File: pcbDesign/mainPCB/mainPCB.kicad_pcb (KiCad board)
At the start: 4 copper layers, 188.1 x 90 mm, 40 parts, among them CN1 CONN 45P FOR GG 01, CN3 WIRE HARN SP FOR GG, CN4 CN4, SW1 UP, SW2 DOWN, SW3 LEFT, SW4 RIGHT, SW5 TL, SW6 TR, SW7 PS, T1 Transformer T1

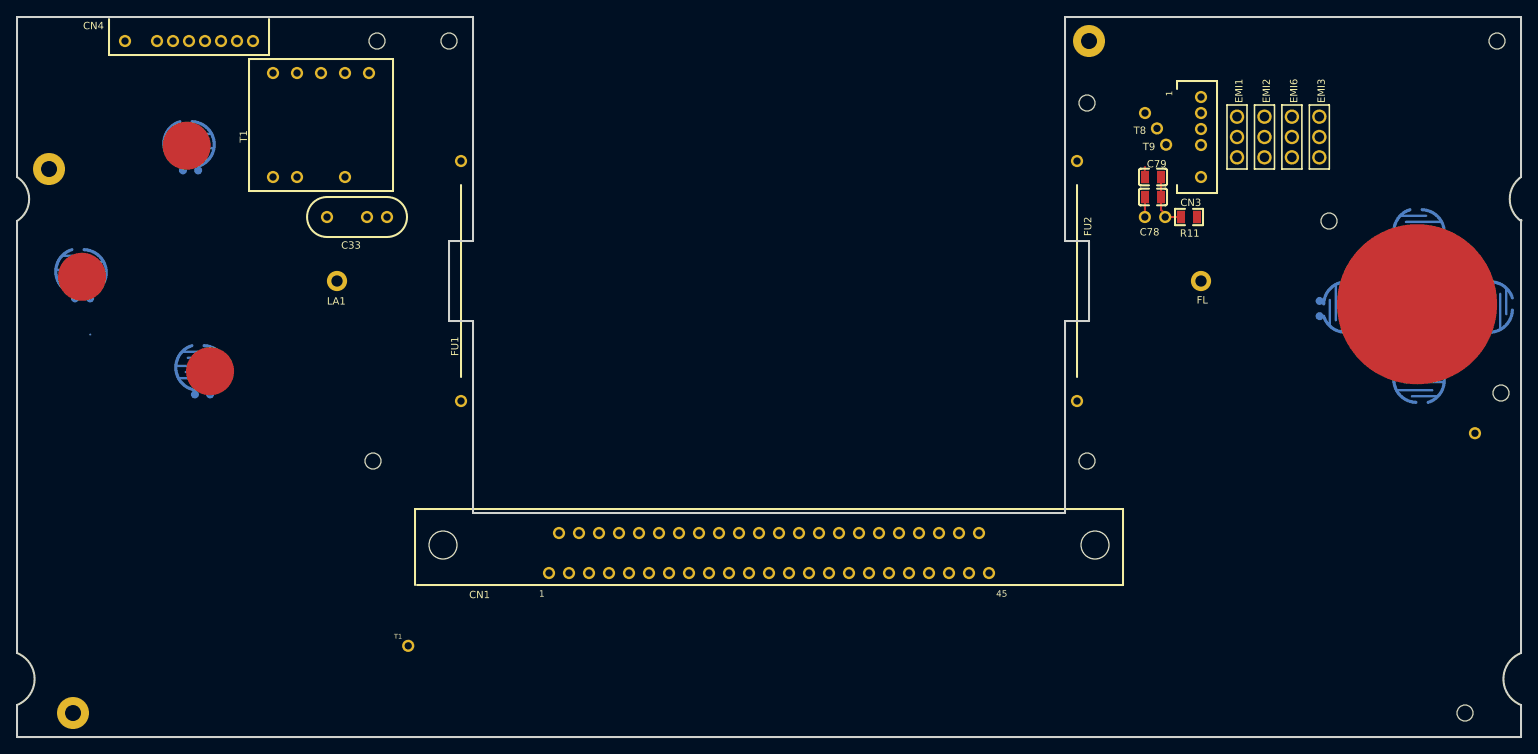
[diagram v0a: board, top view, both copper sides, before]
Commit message: fixed error in pcb border
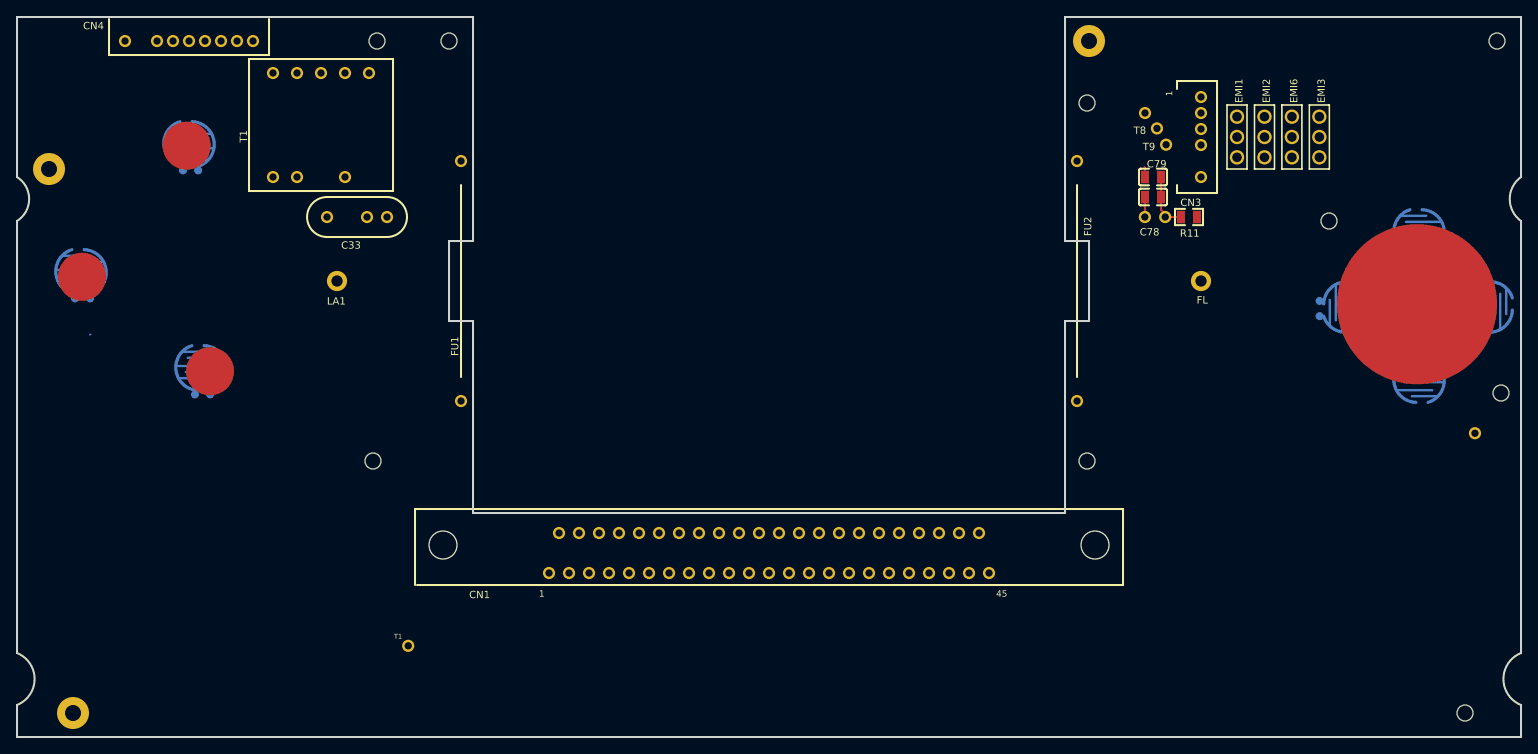
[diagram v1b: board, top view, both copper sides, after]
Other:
- board size 188.1 x 90 mm -> 188 x 90 mm
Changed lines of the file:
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@@
-	)
-	(gr_line
-		(start 50 150)
-		(end 238.0007 150)
-		(stroke
-			(width 0.254)
-			(type default)
-		)
-		(layer "Edge.Cuts")
 	)
 	(gr_line
@@
 		(stroke
 			(width 0.254)
-			(type default)
-		)
-		(layer "Edge.Cuts")
-	)
-	(gr_arc
-		(start 237.96 85.357)
-		(mid 238.0514 85.4078)
-		(end 238.0006 85.4992)
-		(stroke
-			(width 0.254)
